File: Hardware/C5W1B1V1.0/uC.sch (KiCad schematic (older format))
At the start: 47 parts, among them J3 Conn_01x13_Male, SW1 SW_Push_Dual, SW2 SW_Push_Dual, U1 STM32H735IGT6, Y1 ECS-250-8-36CKM-TR3, Y2 830106545501

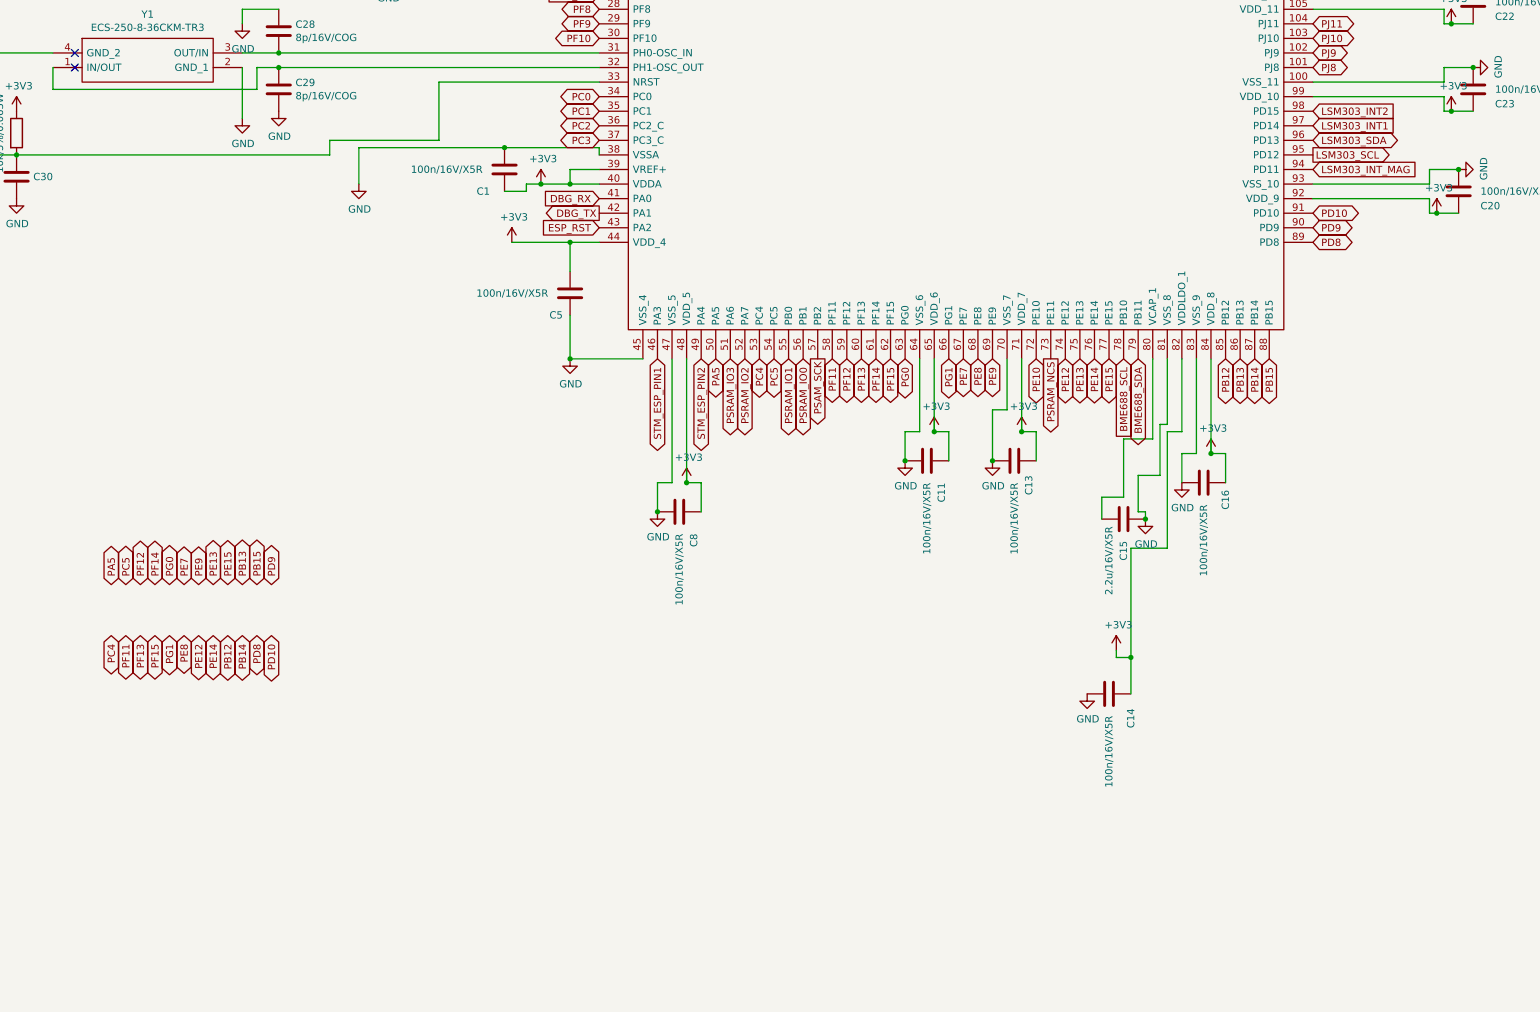
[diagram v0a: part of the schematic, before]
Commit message: Linie PC0-PE13
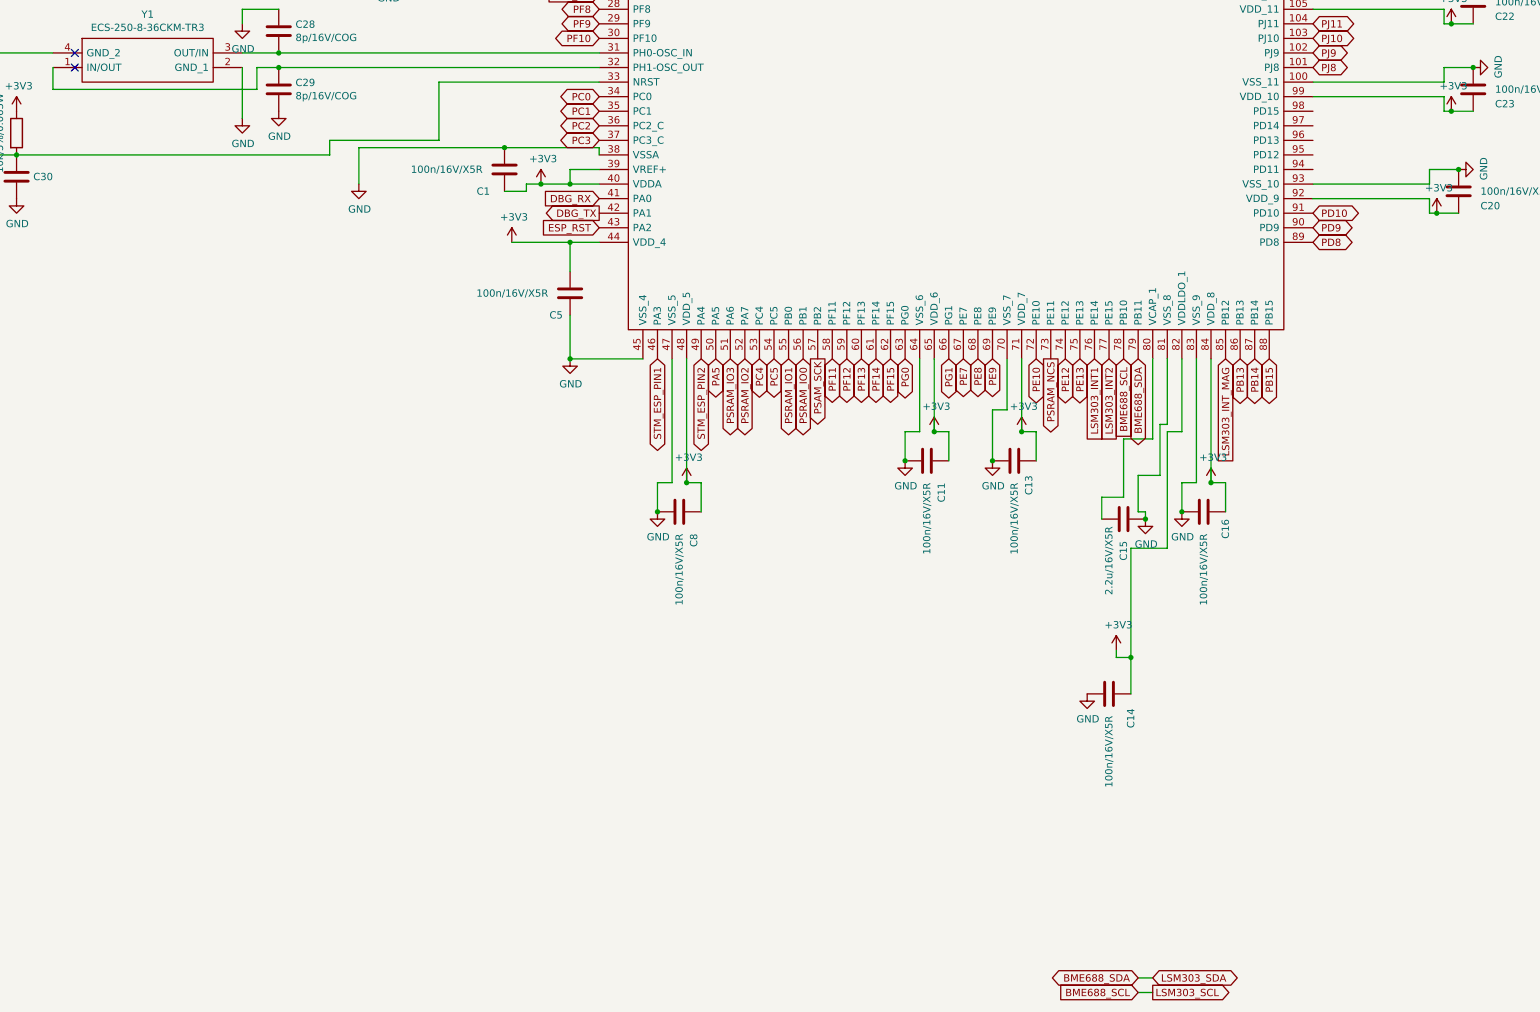
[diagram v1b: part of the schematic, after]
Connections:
- net PB12 is gone; now on net LSM303_INT_MAG: U1.85 (PB12)
- net PE14 is gone; now on net LSM303_INT1: U1.76 (PE14)
- net PE15 is gone; now on net LSM303_INT2: U1.77 (PE15)
- net LSM303_INT1: no longer U1.97 (PD14)
- net LSM303_INT2: no longer U1.98 (PD15)
- net LSM303_INT_MAG: no longer U1.94 (PD11)
- net LSM303_SCL: no longer names the net of U1.95 (PD12)
- net LSM303_SDA: no longer names the net of U1.96 (PD13)
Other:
- moved on the sheet: C16
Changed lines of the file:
@@
 L Device:C C16
 U 1 1 666073E1
-P 12950 11950
-F 0 "C16" H 13000 12100 50  0000 L CNN
-F 1 "100n/16V/X5R" H 13100 11950 50  0000 L CNN
-F 2 "Capacitor_SMD:C_0402_1005Metric" H 12988 11800 50  0001 C CNN
-F 3 "~" H 12950 11950 50  0001 C CNN
-	1    12950 11950
+P 12950 12150
+F 0 "C16" H 13000 12300 50  0000 L CNN
+F 1 "100n/16V/X5R" H 13100 12150 50  0000 L CNN
+F 2 "Capacitor_SMD:C_0402_1005Metric" H 12988 12000 50  0001 C CNN
+F 3 "~" H 12950 12150 50  0001 C CNN
+	1    12950 12150
 	0    1    1    0
 $EndComp
 Wire Wire Line
-	12900 11750 12800 11750
-Wire Wire Line
-	12800 11750 12800 11950
-Wire Wire Line
-	13000 11750 13100 11750
-Wire Wire Line
-	13100 11750 13100 11950
+	12900 11950 12800 11950
+Wire Wire Line
+	12800 11950 12800 12150
+Wire Wire Line
+	13000 11950 13100 11950
+Wire Wire Line
+	13100 11950 13100 12150
 $Comp
 L power:+3V3 #PWR0119
 U 1 1 666073ED
-P 13000 11750
-F 0 "#PWR0119" H 13000 11600 50  0001 C CNN
-F 1 "+3V3" H 13015 11923 50  0000 C CNN
-F 2 "" H 13000 11750 50  0001 C CNN
-F 3 "" H 13000 11750 50  0001 C CNN
-	1    13000 11750
-	1    0    0    -1
-$EndComp
-Wire Wire Line
-	12900 11100 12900 11750
-Wire Wire Line
-	13000 11100 13000 11750
+P 13000 11950
+F 0 "#PWR0119" H 13000 11800 50  0001 C CNN
+F 1 "+3V3" H 13015 12123 50  0000 C CNN
+F 2 "" H 13000 11950 50  0001 C CNN
+F 3 "" H 13000 11950 50  0001 C CNN
+	1    13000 11950
+	1    0    0    -1
+$EndComp
 $Comp
 L Device:C C20
@@
 Connection ~ 11100 11600
 Connection ~ 11500 11800
-Connection ~ 13000 11750
+Connection ~ 13000 11950
 Connection ~ 13450 4450
 Wire Notes Line
@@
 L power:GND #PWR0172
 U 1 1 67C3691E
-P 12800 11950
-F 0 "#PWR0172" H 12800 11700 50  0001 C CNN
-F 1 "GND" H 12805 11777 50  0000 C CNN
-F 2 "" H 12800 11950 50  0001 C CNN
-F 3 "" H 12800 11950 50  0001 C CNN
-	1    12800 11950
+P 12800 12150
+F 0 "#PWR0172" H 12800 11900 50  0001 C CNN
+F 1 "GND" H 12805 11977 50  0000 C CNN
+F 2 "" H 12800 12150 50  0001 C CNN
+F 3 "" H 12800 12150 50  0001 C CNN
+	1    12800 12150
 	1    0    0    -1
 $EndComp
@@
 Text GLabel 8800 8500 0    50   Output ~ 0
 ESP_TX
-Text GLabel 12300 11100 3    50   BiDi ~ 0
-PE15
-Text GLabel 12200 11100 3    50   BiDi ~ 0
-PE14
 Text GLabel 12100 11100 3    50   BiDi ~ 0
 PE13
@@
 Text GLabel 9600 11100 3    50   BiDi ~ 0
 PA5
-Text GLabel 12500 11100 3    50   BiDi ~ 0
+Text GLabel 12500 15350 0    50   BiDi ~ 0
 BME688_SDA
-Text GLabel 12400 11100 3    50   Input ~ 0
+Text GLabel 12500 15450 0    50   Input ~ 0
 BME688_SCL
-Text GLabel 13100 11100 3    50   BiDi ~ 0
-PB12
 Text GLabel 13200 11100 3    50   BiDi ~ 0
 PB13
@@
 Text GLabel 9800 5200 1    50   BiDi ~ 0
 PB9
-Text GLabel 13700 9700 2    50   Output ~ 0
+Text GLabel 12600 15450 2    50   Output ~ 0
 LSM303_SCL
-Text GLabel 13700 9600 2    50   BiDi ~ 0
-LSM303_SDA
-Text GLabel 13700 9800 2    50   Input ~ 0
+Text GLabel 13100 11100 3    50   Input ~ 0
 LSM303_INT_MAG
-Text GLabel 13700 9500 2    50   Input ~ 0
-LSM303_INT1
-Text GLabel 13700 9400 2    50   Input ~ 0
+Text GLabel 12300 11100 3    50   Input ~ 0
 LSM303_INT2
-Text GLabel 5450 12650 1    50   BiDi ~ 0
-PA5
-Text GLabel 5450 13000 3    50   BiDi ~ 0
-PC4
-Text GLabel 5550 12650 1    50   BiDi ~ 0
-PC5
-Text GLabel 5550 13000 3    50   BiDi ~ 0
-PF11
-Text GLabel 5650 12650 1    50   BiDi ~ 0
-PF12
-Text GLabel 5650 13000 3    50   BiDi ~ 0
-PF13
-Text GLabel 5750 12650 1    50   BiDi ~ 0
-PF14
-Text GLabel 5750 13000 3    50   BiDi ~ 0
-PF15
-Text GLabel 5850 12650 1    50   BiDi ~ 0
-PG0
-Text GLabel 6050 12650 1    50   BiDi ~ 0
-PE9
-Text GLabel 5950 13000 3    50   BiDi ~ 0
-PE8
-Text GLabel 5950 12650 1    50   BiDi ~ 0
-PE7
-Text GLabel 5850 13000 3    50   BiDi ~ 0
-PG1
-Text GLabel 6250 12650 1    50   BiDi ~ 0
-PE15
-Text GLabel 6150 13000 3    50   BiDi ~ 0
-PE14
-Text GLabel 6150 12650 1    50   BiDi ~ 0
-PE13
-Text GLabel 6050 13000 3    50   BiDi ~ 0
-PE12
-Text GLabel 6250 13000 3    50   BiDi ~ 0
-PB12
-Text GLabel 6350 12650 1    50   BiDi ~ 0
-PB13
-Text GLabel 6350 13000 3    50   BiDi ~ 0
-PB14
-Text GLabel 6450 12650 1    50   BiDi ~ 0
-PB15
 Connection ~ 9200 12150
 Text GLabel 13700 10300 2    50   BiDi ~ 0
@@
 Text GLabel 13700 10100 2    50   BiDi ~ 0
 PD10
-Text GLabel 6450 13000 3    50   BiDi ~ 0
-PD8
-Text GLabel 6550 12650 1    50   BiDi ~ 0
-PD9
-Text GLabel 6550 13000 3    50   BiDi ~ 0
-PD10
+Text GLabel 12200 11100 3    50   Input ~ 0
+LSM303_INT1
+Text GLabel 12600 15350 2    50   BiDi ~ 0
+LSM303_SDA
+Wire Wire Line
+	12500 15350 12600 15350
+Wire Wire Line
+	12500 15450 12600 15450
+Text GLabel 12500 11100 3    50   BiDi ~ 0
+BME688_SDA
+Text GLabel 12400 11100 3    50   Input ~ 0
+BME688_SCL
+Connection ~ 12800 12150
+Wire Wire Line
+	12900 11100 12900 11950
+Wire Wire Line
+	13000 11100 13000 11950
 $EndSCHEMATC

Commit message: Rozlana masa
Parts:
- added C57, C58, C59: 100n/16V/X5R, Capacitor_SMD:C_0402_1005Metric, symbol Device:C
- added D4, D5: LED, LED_SMD:LED_0805_2012Metric, symbol Device:LED
- added D6: WS2812B, LED_SMD:LED_WS2812B_PLCC4_5.0x5.0mm_P3.2mm, symbol LED:WS2812B
- added J7: Conn_01x02_Male, Connector_PinHeader_2.54mm:PinHeader_1x02_P2.54mm_Vertical, symbol Connector:Conn_01x02_Male
- added R18, R19: 10k/5%/0.063W, Resistor_SMD:R_0402_1005Metric, symbol Device:R
- added R26, R27, R28: 470/5%/0.063W, Resistor_SMD:R_0402_1005Metric, symbol Device:R
- added SW5, SW6: SW_Push_Dual, Button_Switch_SMD:SW_Push_1P1T_NO_6x6mm_H9.5mm, symbol Switch:SW_Push_Dual
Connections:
- net +3V3: now also R18.1, R19.1
- net +5V: now also C59.1, D6.1 (VDD)
- net GND: now also C57.1, C58.1, C59.2, D4.1 (K), D5.1 (K), D6.3 (VSS), J7.2 (Pin_2), SW5.2, SW5.4, SW6.2, SW6.4
- net SSD1331_DC: now also U1.3 (PE4); no longer U1.2 (PE3)
- net SSD1331_RES: now also U1.2 (PE3); no longer U1.3 (PE4)
- net VBAT: now also J7.1 (Pin_1)
- net PD11: now reaches U1.94 (PD11)
- net PD12: now reaches U1.95 (PD12)
- net PD13: now reaches U1.96 (PD13)
- net PD14: now reaches U1.97 (PD14)
- net PD15: now reaches U1.98 (PD15)
- net PC0 renamed 12V_DC_V
- net PC1 renamed 12V_EN
- net PC6 renamed WS2812
- net WS2812: now also R26.2
- net PG5 renamed BUTTON2
- net BUTTON2: now also C58.2, R19.2, SW6.1, SW6.3
- net PG6 renamed BUTTON1
- net BUTTON1: now also C57.2, R18.2, SW5.1, SW5.3
- net PG7 renamed LED2
- net LED2: now also R28.2
- net PG8 renamed LED1
- net LED1: now also R27.2
- new net: D6.4 (DIN), R26.1
- new net: D4.2 (A), R27.1
- new net: D5.2 (A), R28.1
